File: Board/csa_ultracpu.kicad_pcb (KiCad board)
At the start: 4 copper layers, 160 x 100 mm, 182 parts, among them IC1 74LVC125, IC13 74244DW, IC14 74LVC14, IC16 74LVC8T245SO24, IC18 74LVC06, IC19 74244DW, IC4 74HCT245DW, IC5 74HCT245DW, IC6 741G04DBV, IC8 MAX3421E, J1 HDMI_A, J2 Micro_SD_Card_Det2, P1 CSABUS, Q2 32kHz, Q3 12MHz, U1 IS61WV51216EDALL, U2 74LVC125, U4 XC6SLX25-CSG324, U5 IS61WV51216EDALL, X1 SJ1-3513N, X3 SG-8002CE

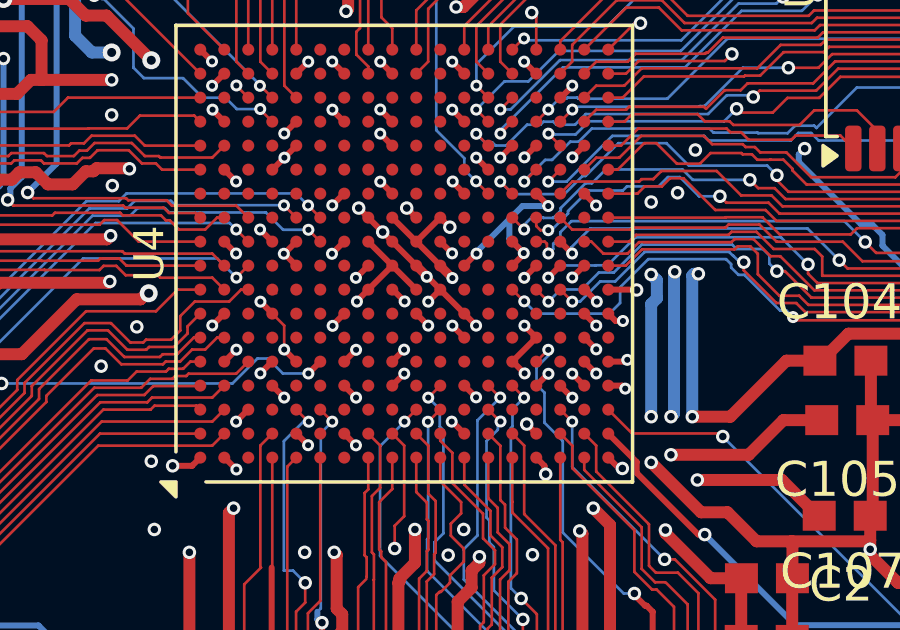
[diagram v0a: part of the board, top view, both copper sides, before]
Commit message: fix a few vias under bga
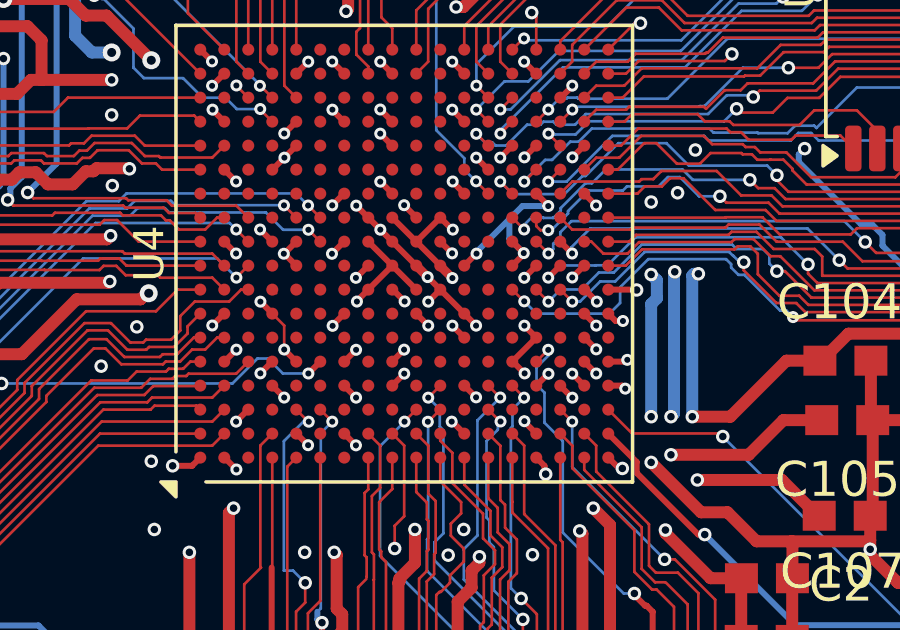
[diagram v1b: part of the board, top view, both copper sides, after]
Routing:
- net V12: track 223.8 -> 222.4 mm

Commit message: test release
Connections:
- JP7 pad 2: /CPU,RAM,ROM/ABORTB -> /ABORT
- R10 pad 2: /CPU,RAM,ROM/ABORTB -> /ABORT
- U$1 pad 4: /CPU,RAM,ROM/ABORTB -> /ABORT
- U4 pad C2: unconnected-(U4B-IO_L83P_3-PadC2) -> /ABORT
- U4 pad F16: unconnected-(U4A-IO_L1N_A24_VREF_1-PadF16) -> /NMI
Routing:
- net /ABORT: track 0.00 -> 98.2 mm, vias 0 -> 8
- net /NMI: track 115.7 -> 163.2 mm, vias 3 -> 8
- net /CPU,RAM,ROM/ABORTB: track 26.6 -> 0.00 mm, vias 2 -> 0
- net /IRQ: track 250.7 -> 250.2 mm
- net SYNC: track 71.2 -> 70.7 mm
